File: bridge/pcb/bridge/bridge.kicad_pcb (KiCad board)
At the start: 2 copper layers, 160 x 80 mm, 30 parts, among them J1 Screw_Terminal_01x06, J2 Screw_Terminal_01x06, J3 Screw_Terminal_01x06, J4 Conn_01x23, Q1 PMOS, Q2 PMOS, Q3 PMOS, Q4 PMOS, Q5 PMOS, SW1 SW_SPST, U1 YAAJ_BluePill, U2 J104D2C12VDC.20S, U3 AD557JN

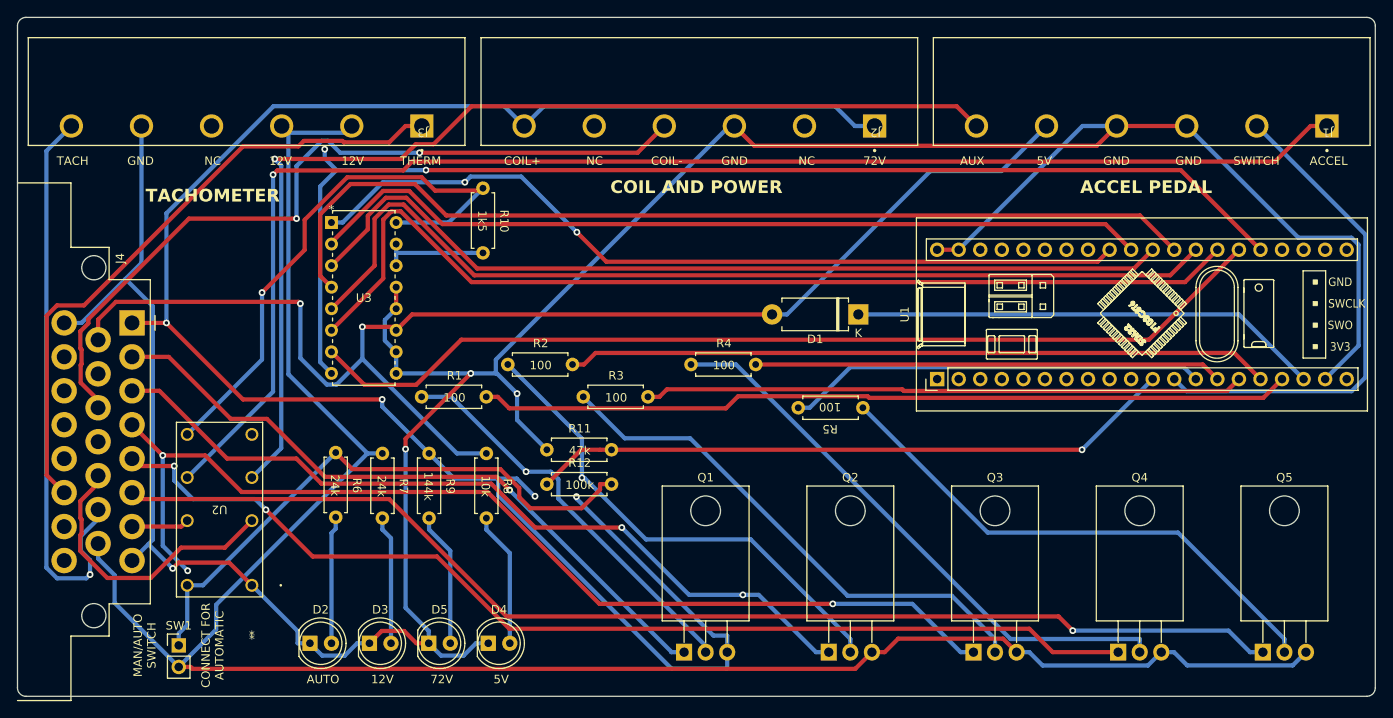
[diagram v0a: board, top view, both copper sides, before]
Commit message: Started fixing PCB, reduced footprint and changed MCU
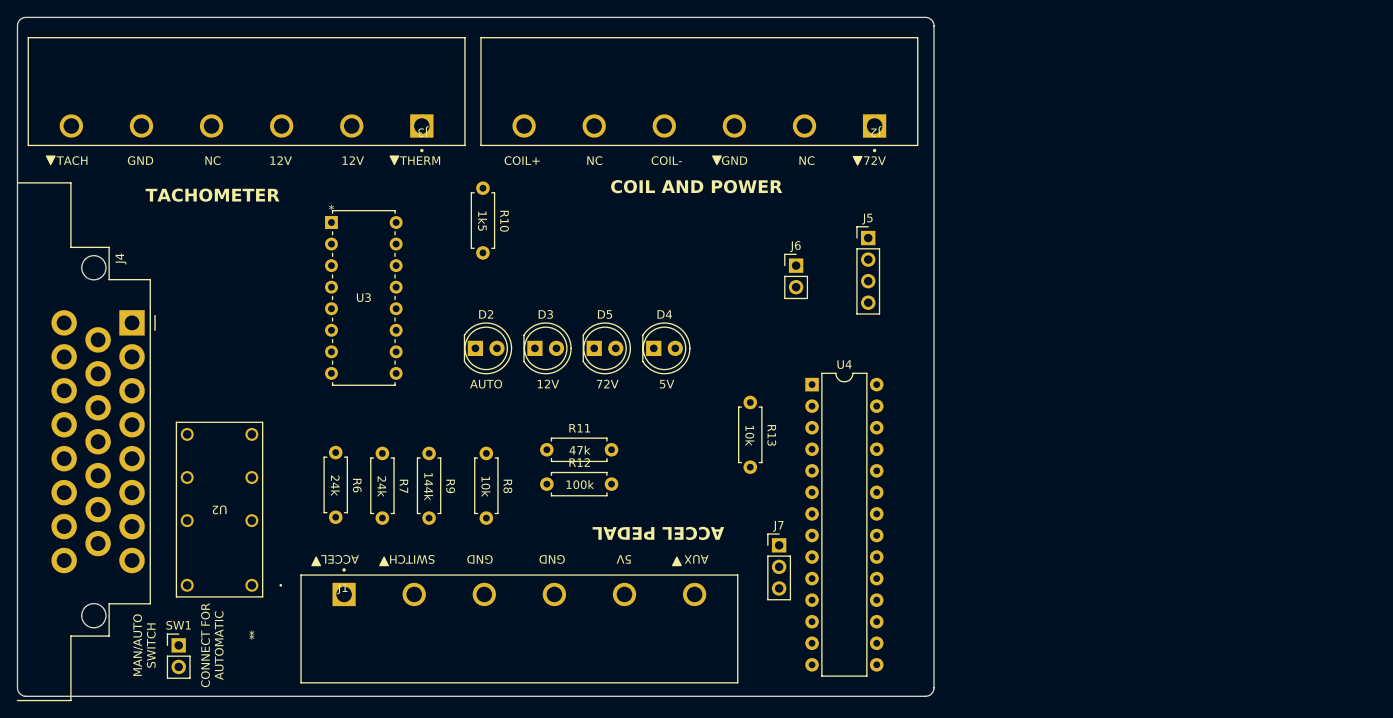
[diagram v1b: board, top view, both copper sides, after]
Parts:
- removed D1: D, Diode_THT:D_DO-15_P10.16mm_Horizontal
- removed Q1, Q2, Q3, Q4, Q5: PMOS, Package_TO_SOT_THT:TO-220-3_Horizontal_TabDown
- removed R1, R2, R3, R4, R5: 100, bridge:THT_RESISTOR_WITH_VALUE
- removed U1: YAAJ_BluePill, bridge:YAAJ_BluePill_1
- added J5: Conn_01x04, Connector_PinHeader_2.54mm:PinHeader_1x04_P2.54mm_Vertical, F.Cu at (163.2, 67.0)
- added J6: Conn_01x02, Connector_PinHeader_2.54mm:PinHeader_1x02_P2.54mm_Vertical, F.Cu at (154.8, 70.2)
- added J7: Conn_01x03, Connector_PinHeader_2.54mm:PinHeader_1x03_P2.54mm_Vertical, F.Cu at (152.8, 103.2)
- added R13: 10k, bridge:THT_RESISTOR_WITH_VALUE, F.Cu at (149.2, 90.2)
- added U4: ATmega328P-P, Package_DIP:DIP-28_W7.62mm, F.Cu at (156.6, 84.3)
- moved J1 128.5 mm to (101.4, 109.0), turned to 0 degrees
- moved D5 39.8 mm to (131.0, 80.0)
- moved D2 39.8 mm to (117.0, 80.0)
- moved D3 39.8 mm to (124.0, 80.0)
- moved D4 39.8 mm to (138.0, 80.0)
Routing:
- net GND: track 351.4 -> 0.00 mm, vias 4 -> 0
- net +12V: track 242.8 -> 0.00 mm
- net +BATT: track 226.9 -> 0.00 mm, vias 4 -> 0
- net ACCEL_MAN: track 166.4 -> 0.00 mm, vias 1 -> 0
- net +5V: track 157.2 -> 0.00 mm, vias 2 -> 0
- net Net-(U3-(MSB)BIT1): track 141.1 -> 0.00 mm, vias 2 -> 0
- net TURF_SWITCH: track 141.0 -> 0.00 mm, vias 1 -> 0
- net REVERSE_SWITCH: track 126.6 -> 0.00 mm, vias 2 -> 0
- net ACCEL_AUX_MAN: track 125.5 -> 0.00 mm, vias 1 -> 0
- net FORWARD_SWITCH: track 125.1 -> 0.00 mm, vias 3 -> 0
- net Net-(U3-BIT3): track 119.3 -> 0.00 mm
- net Net-(U3-BIT2): track 115.1 -> 0.00 mm
- net Net-(U3-BIT4): track 114.9 -> 0.00 mm
- net Net-(U3-BIT5): track 114.5 -> 0.00 mm
- net Net-(U3-BIT6): track 105.4 -> 0.00 mm
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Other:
- board size 160 x 80 mm -> 108 x 80 mm

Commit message: Completed basic functionality PCB
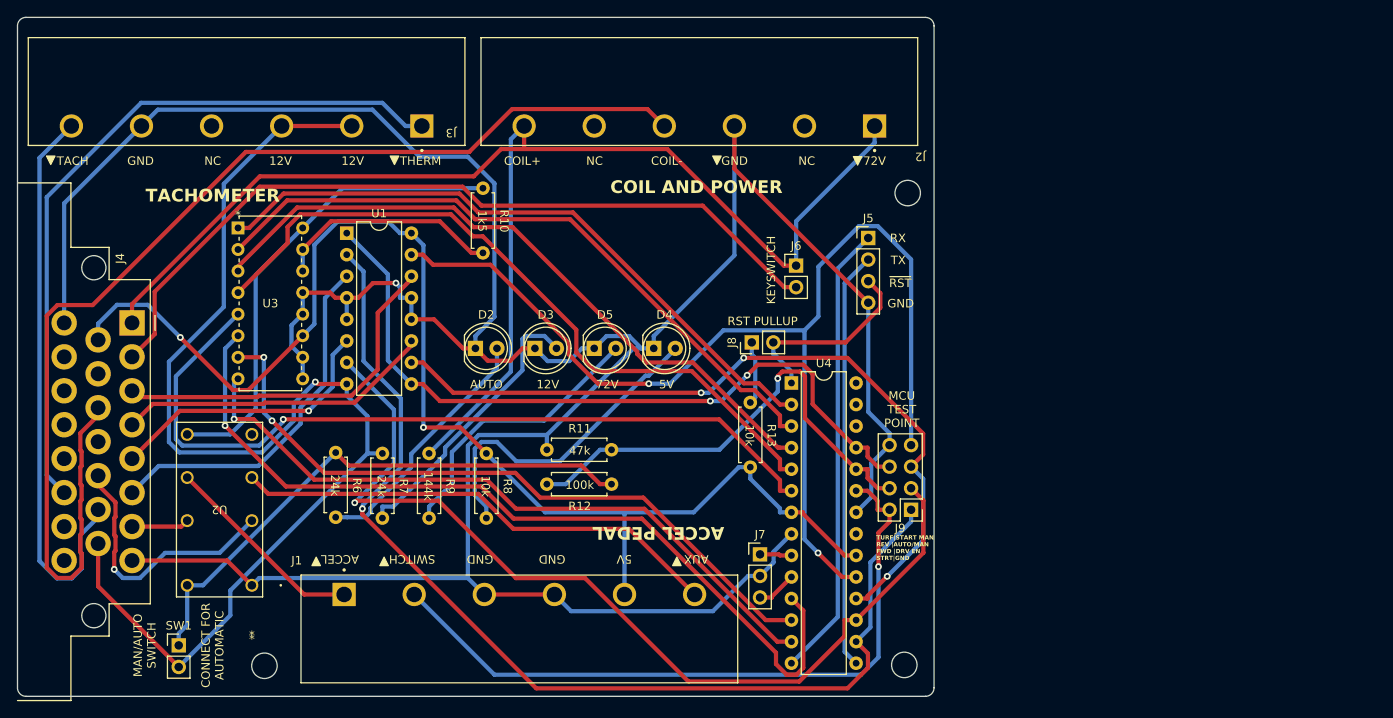
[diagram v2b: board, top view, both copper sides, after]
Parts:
- added J8: Conn_01x02, Connector_PinHeader_2.54mm:PinHeader_1x02_P2.54mm_Vertical, F.Cu at (149.5, 79.3)
- added J9: MCU_Test_Point, Connector_PinHeader_2.54mm:PinHeader_2x04_P2.54mm_Vertical, F.Cu at (168.3, 99.0)
- added U1: L293, Package_DIP:DIP-16_W7.62mm, F.Cu at (101.8, 66.4)
- moved U3 11.0 mm to (89.0, 65.8)
- moved J7 2.49 mm to (150.5, 104.3)
- moved U4 2.44 mm to (154.2, 84.1)
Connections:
- R13 pad 1: Net-(J5-Pin_3) -> Net-(J8-Pin_1)
- U4 pad 25: unconnected-(U4-PC2-Pad25) -> DRV_ENABLE
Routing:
- net GND: track 0.00 -> 371.3 mm, vias 0 -> 1
- net +BATT: track 0.00 -> 159.9 mm
- net +5V: track 0.00 -> 154.1 mm, vias 0 -> 2
- net +12V: track 0.00 -> 141.0 mm, vias 0 -> 1
- net COIL_CONTROL_GND: track 0.00 -> 138.6 mm
- net MCU_START: track 0.00 -> 133.2 mm, vias 0 -> 2
- net MCU_TURF: track 0.00 -> 126.1 mm, vias 0 -> 1
- net MCU_REVERSE: track 0.00 -> 112.3 mm, vias 0 -> 1
- net Net-(U3-BIT3): track 0.00 -> 101.4 mm, vias 0 -> 1
- net Net-(U3-BIT4): track 0.00 -> 96.3 mm, vias 0 -> 1
- net KEYSWITCH: track 0.00 -> 94.4 mm
- net MCU_FORWARD: track 0.00 -> 91.9 mm, vias 0 -> 3
- net DRV_ENABLE: track 0.00 -> 87.6 mm, vias 0 -> 2
- net THERMOSTAT: track 0.00 -> 85.6 mm
- net Net-(U3-BIT5): track 0.00 -> 84.8 mm
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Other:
- outline, holes or cut-outs redrawn
- board text added: "KEYSWITCH"
- board text added: "MCU TEST POINT"
- board text added: "RST PULLUP"
- board text added: "RX"
- board text added: "TURF|START MAN REV |AUTO/MAN FWD |DRV EN STRT|GND"
- board text added: "TX"
- board text added: "~{RST}"

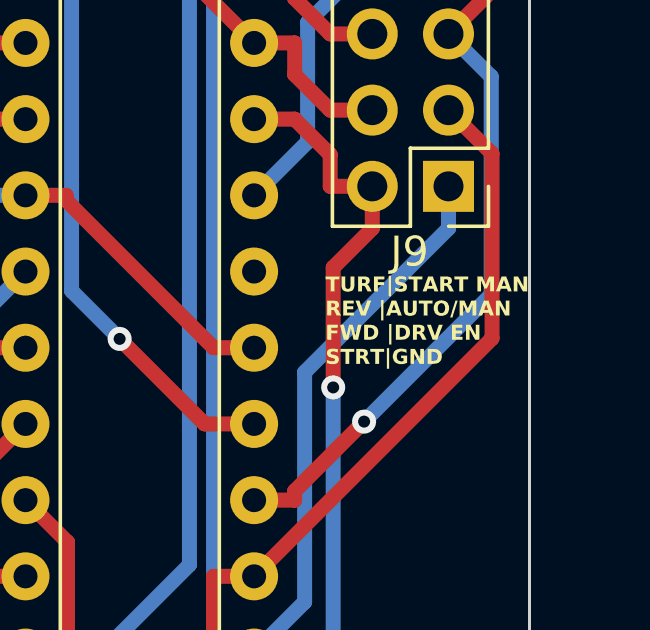
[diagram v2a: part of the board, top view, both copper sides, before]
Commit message: Fixed incorrect test point labeling
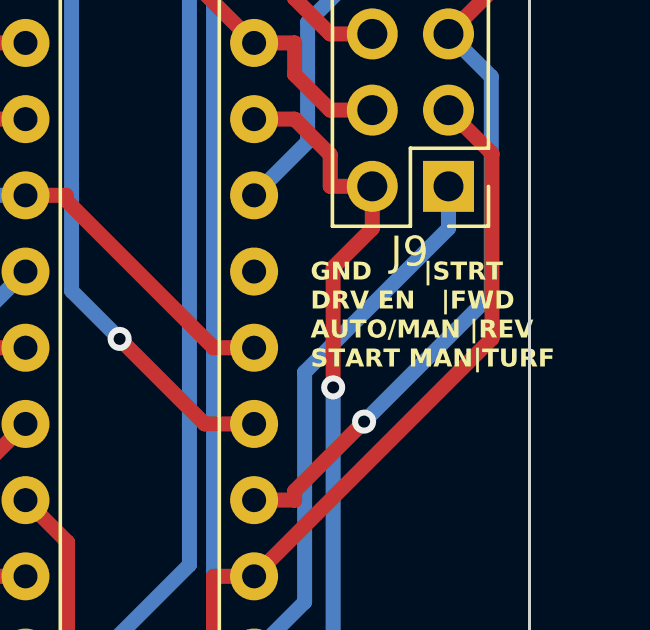
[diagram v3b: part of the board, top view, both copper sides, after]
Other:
- board text added: "GND |STRT DRV EN |FWD AUTO/MAN |REV START MAN|TURF"
- board text removed: "TURF|START MAN REV |AUTO/MAN FWD |DRV EN STRT|GND"

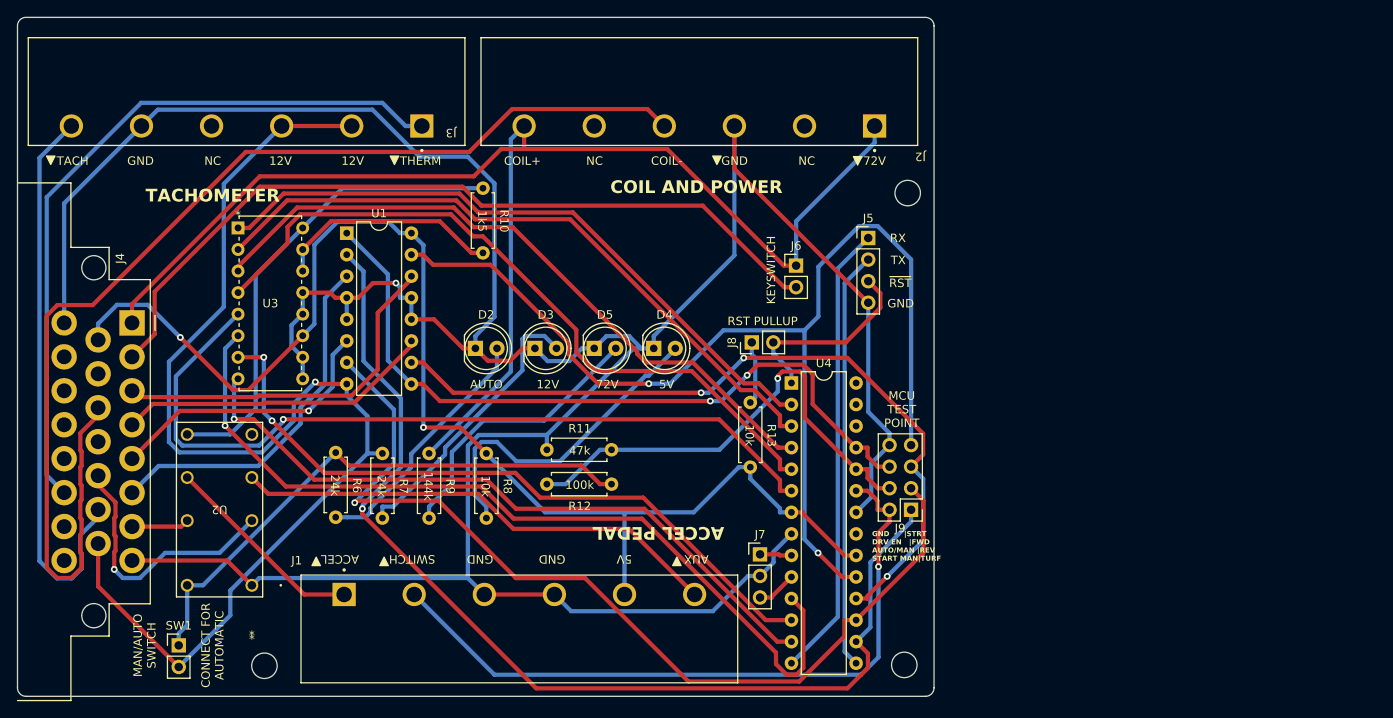
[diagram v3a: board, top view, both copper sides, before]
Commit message: Fixed PORTB and PORTD of atmega328p being reversed
Changed RST pin on uart header to be 5V instead and adjusted labels accordingly
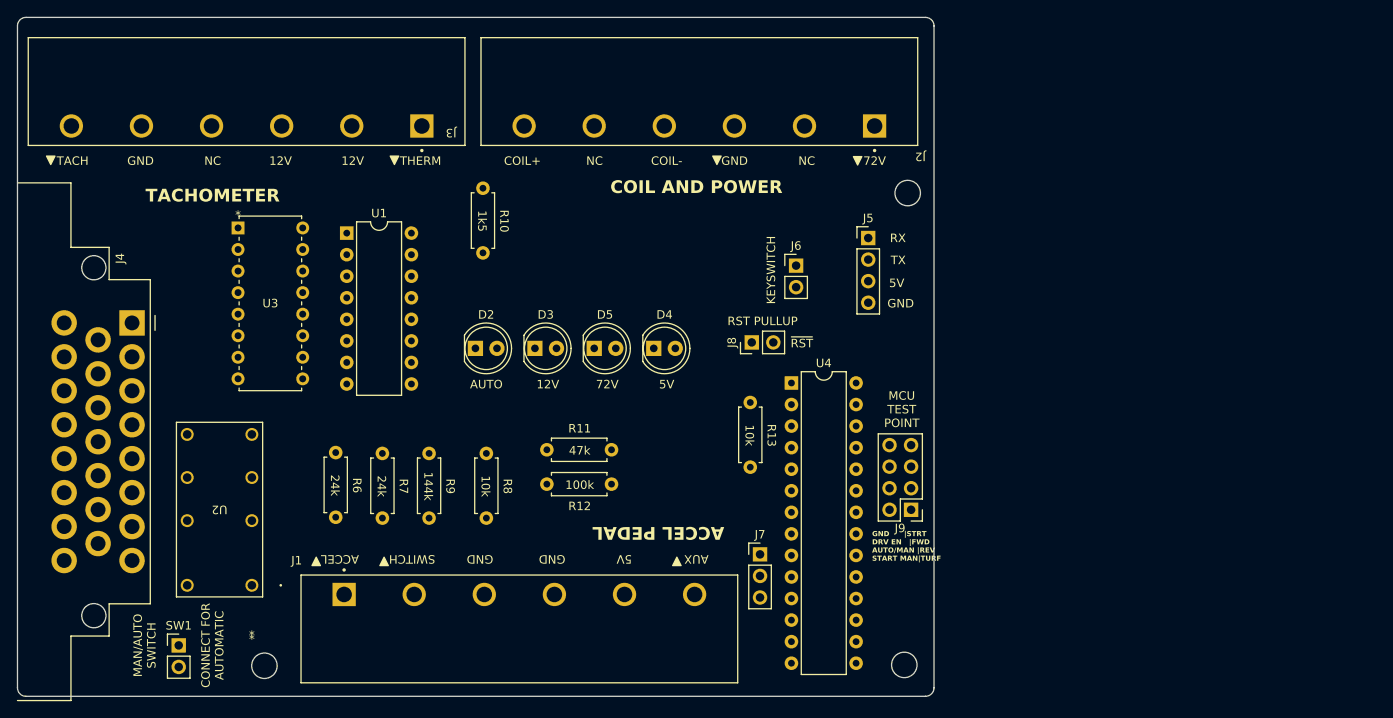
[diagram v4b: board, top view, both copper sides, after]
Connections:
- J5 pad 3: Net-(J5-Pin_3) -> +5V
- J8 pad 2: Net-(J5-Pin_3) -> Net-(J8-Pin_2)
- U3 pad 2: Net-(U3-BIT7) -> Net-(U3-(LSB)BIT8)
- U3 pad 3: Net-(U3-BIT6) -> Net-(U3-(LSB)BIT8)
- U4 pad 1: Net-(J5-Pin_3) -> Net-(J8-Pin_2)
- U4 pad 11: Net-(U3-BIT3) -> MCU_START
- U4 pad 12: Net-(U3-BIT2) -> DRV_ENABLE
- U4 pad 13: Net-(U3-(MSB)BIT1) -> unconnected-(U4-PD7-Pad13)
- U4 pad 14: Net-(J5-Pin_1) -> Net-(U3-(LSB)BIT8)
- U4 pad 15: Net-(J5-Pin_2) -> Net-(U3-BIT5)
- U4 pad 16: MCU_TURF -> Net-(U3-BIT4)
- U4 pad 17: MCU_REVERSE -> Net-(U3-BIT3)
- U4 pad 18: MCU_FORWARD -> Net-(U3-BIT2)
- U4 pad 19: MCU_START -> Net-(U3-(MSB)BIT1)
- U4 pad 2: Net-(U3-(LSB)BIT8) -> Net-(J5-Pin_1)
- U4 pad 25: DRV_ENABLE -> unconnected-(U4-PC2-Pad25)
- U4 pad 3: Net-(U3-BIT7) -> Net-(J5-Pin_2)
- U4 pad 4: Net-(U3-BIT6) -> MCU_TURF
- U4 pad 5: Net-(U3-BIT5) -> MCU_REVERSE
- U4 pad 6: Net-(U3-BIT4) -> MCU_FORWARD
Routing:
- net GND: track 371.3 -> 0.00 mm, vias 1 -> 0
- net +BATT: track 159.9 -> 0.00 mm
- net +5V: track 154.1 -> 0.00 mm, vias 2 -> 0
- net +12V: track 141.0 -> 0.00 mm, vias 1 -> 0
- net COIL_CONTROL_GND: track 138.6 -> 0.00 mm
- net MCU_START: track 133.2 -> 0.00 mm, vias 2 -> 0
- net MCU_TURF: track 126.1 -> 0.00 mm, vias 1 -> 0
- net MCU_REVERSE: track 112.3 -> 0.00 mm, vias 1 -> 0
- net Net-(U3-BIT3): track 101.4 -> 0.00 mm, vias 1 -> 0
- net Net-(U3-BIT4): track 96.3 -> 0.00 mm, vias 1 -> 0
- net KEYSWITCH: track 94.4 -> 0.00 mm
- net MCU_FORWARD: track 91.9 -> 0.00 mm, vias 3 -> 0
- net DRV_ENABLE: track 87.6 -> 0.00 mm, vias 2 -> 0
- net THERMOSTAT: track 85.6 -> 0.00 mm
- net Net-(U3-BIT5): track 84.8 -> 0.00 mm
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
